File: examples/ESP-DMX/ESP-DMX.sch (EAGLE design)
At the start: 8 parts, among them IC1 MAX481CPA

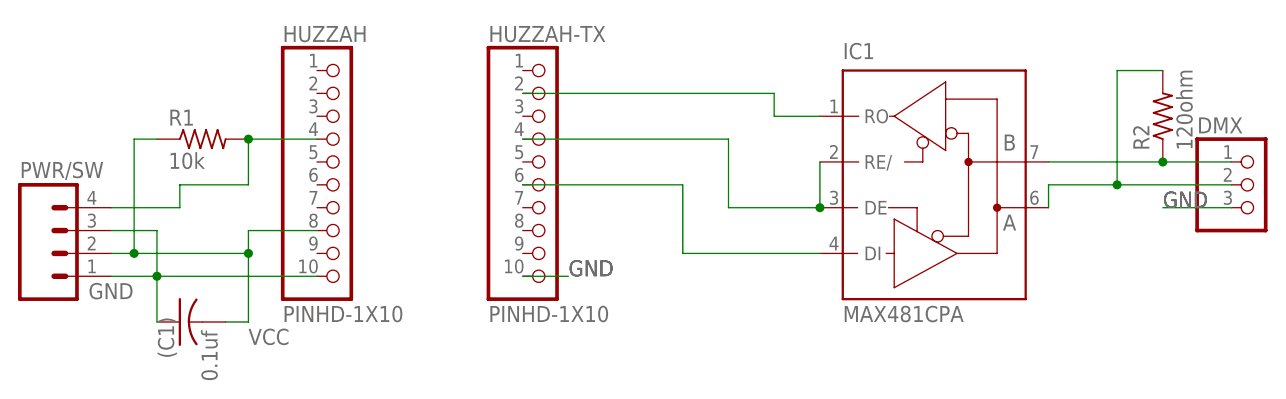
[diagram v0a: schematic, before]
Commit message: Change input pullup resistor
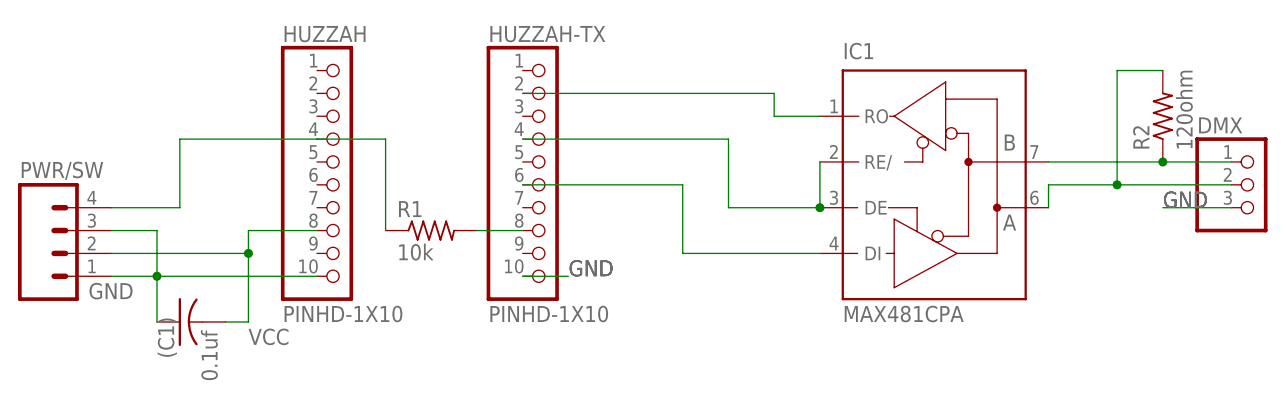
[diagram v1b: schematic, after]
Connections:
- new net N$7: HUZZAH-TX.8, R1.2
- net N$8: now also R1.1; no longer R1.2
- net VCC: no longer R1.1
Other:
- moved on the sheet: R1
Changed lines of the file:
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@@
 <?xml version="1.0" encoding="utf-8"?>
 <!DOCTYPE eagle SYSTEM "eagle.dtd">
-<eagle version="7.5.0">
+<eagle version="7.7.0">
 <drawing>
 <settings>
@@
 <instance part="DMX" gate="A" x="142.24" y="45.72"/>
 <instance part="PWR/SW" gate="G$1" x="10.16" y="38.1"/>
-<instance part="R1" gate="G$1" x="25.4" y="50.8"/>
+<instance part="R1" gate="G$1" x="50.8" y="40.64"/>
 <instance part="R2" gate="G$1" x="132.08" y="53.34" rot="R90"/>
 <instance part="(C1)" gate="G$1" x="22.86" y="30.48" smashed="yes" rot="R90">
@@
 <wire x1="38.1" y1="40.64" x2="30.48" y2="40.64" width="0.1524" layer="91"/>
 <pinref part="PWR/SW" gate="G$1" pin="2"/>
-<wire x1="15.24" y1="38.1" x2="17.78" y2="38.1" width="0.1524" layer="91"/>
-<wire x1="17.78" y1="38.1" x2="30.48" y2="38.1" width="0.1524" layer="91"/>
+<wire x1="15.24" y1="38.1" x2="30.48" y2="38.1" width="0.1524" layer="91"/>
 <wire x1="30.48" y1="38.1" x2="30.48" y2="40.64" width="0.1524" layer="91"/>
-<junction x="17.78" y="38.1"/>
-<wire x1="17.78" y1="38.1" x2="17.78" y2="50.8" width="0.1524" layer="91"/>
-<pinref part="R1" gate="G$1" pin="1"/>
-<wire x1="17.78" y1="50.8" x2="20.32" y2="50.8" width="0.1524" layer="91"/>
 <wire x1="30.48" y1="38.1" x2="30.48" y2="30.48" width="0.1524" layer="91"/>
 <junction x="30.48" y="38.1"/>
@@
 <pinref part="PWR/SW" gate="G$1" pin="4"/>
 <wire x1="15.24" y1="43.18" x2="22.86" y2="43.18" width="0.1524" layer="91"/>
-<wire x1="22.86" y1="43.18" x2="22.86" y2="45.72" width="0.1524" layer="91"/>
-<wire x1="22.86" y1="45.72" x2="30.48" y2="45.72" width="0.1524" layer="91"/>
-<pinref part="R1" gate="G$1" pin="2"/>
+<wire x1="22.86" y1="43.18" x2="22.86" y2="50.8" width="0.1524" layer="91"/>
 <pinref part="HUZZAH" gate="G$1" pin="4"/>
-<wire x1="30.48" y1="50.8" x2="38.1" y2="50.8" width="0.1524" layer="91"/>
-<wire x1="30.48" y1="45.72" x2="30.48" y2="50.8" width="0.1524" layer="91"/>
-<junction x="30.48" y="50.8"/>
+<wire x1="22.86" y1="50.8" x2="38.1" y2="50.8" width="0.1524" layer="91"/>
+<pinref part="R1" gate="G$1" pin="1"/>
+<wire x1="45.72" y1="40.64" x2="45.72" y2="50.8" width="0.1524" layer="91"/>
+<wire x1="38.1" y1="50.8" x2="45.72" y2="50.8" width="0.1524" layer="91"/>
 </segment>
 </net>
@@
 </segment>
 </net>
+<net name="N$7" class="0">
+<segment>
+<pinref part="R1" gate="G$1" pin="2"/>
+<pinref part="HUZZAH-TX" gate="G$1" pin="8"/>
+<wire x1="60.96" y1="40.64" x2="55.88" y2="40.64" width="0.1524" layer="91"/>
+</segment>
+</net>

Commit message: add rdm support
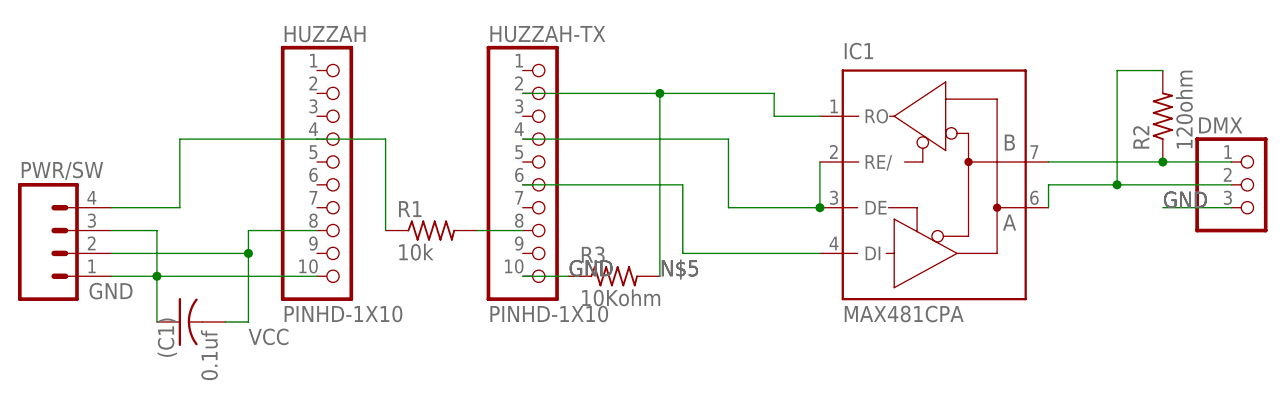
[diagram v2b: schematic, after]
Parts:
- added R3: 10Kohm, RBBB:RESISTOR1/6WATT
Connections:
- net GND: now also R3.1
- net N$5: now also R3.2
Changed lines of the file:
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@@
 <part name="R2" library="RBBB" deviceset="RESISTOR" device="1/6WATT" value="120ohm"/>
 <part name="(C1)" library="resistor" deviceset="C-US" device="050-025X075" value="0.1uf"/>
+<part name="R3" library="RBBB" deviceset="RESISTOR" device="1/6WATT" value="10Kohm"/>
 </parts>
 <sheets>
@@
 <attribute name="VALUE" x="27.051" y="23.876" size="1.778" layer="96" rot="R90"/>
 </instance>
+<instance part="R3" gate="G$1" x="71.12" y="35.56"/>
 </instances>
 <busses>
@@
 <label x="66.04" y="35.56" size="1.778" layer="95"/>
 <label x="66.04" y="35.56" size="1.778" layer="95"/>
+<pinref part="R3" gate="G$1" pin="1"/>
 </segment>
 </net>
@@
 <wire x1="93.98" y1="53.34" x2="88.9" y2="53.34" width="0.1524" layer="91"/>
 <pinref part="HUZZAH-TX" gate="G$1" pin="2"/>
-<wire x1="60.96" y1="55.88" x2="88.9" y2="55.88" width="0.1524" layer="91"/>
+<wire x1="60.96" y1="55.88" x2="76.2" y2="55.88" width="0.1524" layer="91"/>
+<wire x1="76.2" y1="55.88" x2="88.9" y2="55.88" width="0.1524" layer="91"/>
 <wire x1="88.9" y1="55.88" x2="88.9" y2="53.34" width="0.1524" layer="91"/>
+<label x="76.2" y="35.56" size="1.778" layer="95"/>
+<label x="76.2" y="35.56" size="1.778" layer="95"/>
+<pinref part="R3" gate="G$1" pin="2"/>
+<wire x1="76.2" y1="35.56" x2="76.2" y2="55.88" width="0.1524" layer="91"/>
+<junction x="76.2" y="55.88"/>
 </segment>
 </net>
